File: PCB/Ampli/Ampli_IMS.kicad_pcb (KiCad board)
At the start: 2 copper layers, 58.4 x 32 mm, 18 parts, among them J1 5227161-3, J2 5227161-3, J3 Conn_01x03_Male, P1 300K, U1 LMC6081, U2 LMC6081

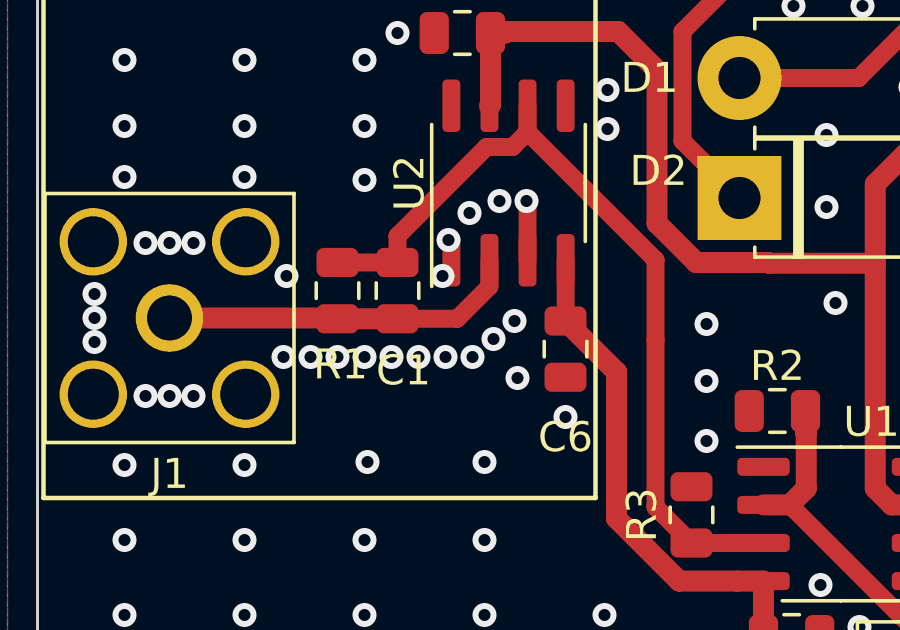
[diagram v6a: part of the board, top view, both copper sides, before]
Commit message: Small mistakes
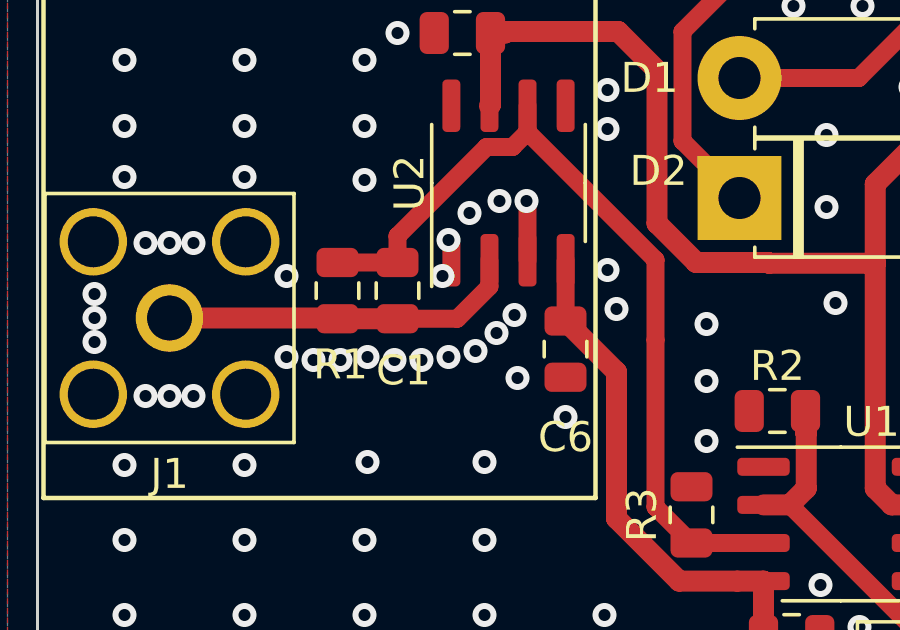
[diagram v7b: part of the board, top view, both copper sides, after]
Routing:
- net GND: vias 151 -> 153
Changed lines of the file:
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@@
     (thickness 1.6)
     (drawings 15)
-    (tracks 228)
+    (tracks 230)
     (zones 0)
     (modules 18)
@@
   )
   (setup
-    (last_trace_width 0.6)
+    (last_trace_width 0.25)
     (user_trace_width 0.4)
     (user_trace_width 0.5)
@@
   (via blind (at 36.6 24.5) (size 0.8) (drill 0.4) (layers F.Cu B.Cu) (net 1))
   (via blind (at 43.6 27.7) (size 0.8) (drill 0.4) (layers F.Cu B.Cu) (net 1))
-  (via (at 36.4 35.3) (size 0.8) (drill 0.4) (layers F.Cu B.Cu) (net 1))
-  (via (at 35.5 35.3) (size 0.8) (drill 0.4) (layers F.Cu B.Cu) (net 1))
+  (via (at 36.5 35.4) (size 0.8) (drill 0.4) (layers F.Cu B.Cu) (net 1))
+  (via (at 35.6 35.3) (size 0.8) (drill 0.4) (layers F.Cu B.Cu) (net 1))
   (via blind (at 79.5 30.3) (size 0.8) (drill 0.4) (layers F.Cu B.Cu) (net 1))
   (via blind (at 75.5 32.8) (size 0.8) (drill 0.4) (layers F.Cu B.Cu) (net 1))
@@
   (segment (start 40.935 32.075) (end 40.935 30.065) (width 0.6) (layer F.Cu) (net 1))
   (segment (start 40.935 30.065) (end 40.935 30.035) (width 0.6) (layer F.Cu) (net 1))
-  (via (at 37.3 35.3) (size 0.8) (drill 0.4) (layers F.Cu B.Cu) (net 1))
-  (via (at 38.2 35.3) (size 0.8) (drill 0.4) (layers F.Cu B.Cu) (net 1))
-  (via (at 39.1 35.3) (size 0.8) (drill 0.4) (layers F.Cu B.Cu) (net 1))
+  (via (at 37.4 35.4) (size 0.8) (drill 0.4) (layers F.Cu B.Cu) (net 1))
+  (via (at 38.3 35.3) (size 0.8) (drill 0.4) (layers F.Cu B.Cu) (net 1))
+  (via (at 39.2 35.1) (size 0.8) (drill 0.4) (layers F.Cu B.Cu) (net 1))
   (via (at 28.2 36.6) (size 0.8) (drill 0.4) (layers F.Cu B.Cu) (net 1))
   (via (at 26.5 33.2) (size 0.8) (drill 0.4) (layers F.Cu B.Cu) (net 1))
@@
   (via blind (at 46.9 34.2) (size 0.8) (drill 0.4) (layers F.Cu B.Cu) (net 1))
   (via blind (at 46.9 36.1) (size 0.8) (drill 0.4) (layers F.Cu B.Cu) (net 1))
-  (via (at 39.8 34.7) (size 0.8) (drill 0.4) (layers F.Cu B.Cu) (net 1))
-  (via (at 34.6 35.3) (size 0.8) (drill 0.4) (layers F.Cu B.Cu) (net 1))
+  (via (at 39.9 34.5) (size 0.8) (drill 0.4) (layers F.Cu B.Cu) (net 1))
+  (via (at 34.7 35.4) (size 0.8) (drill 0.4) (layers F.Cu B.Cu) (net 1))
   (via blind (at 35.5 29.4) (size 0.8) (drill 0.4) (layers F.Cu B.Cu) (net 1))
   (via blind (at 55.1 32.7) (size 0.8) (drill 0.4) (layers F.Cu B.Cu) (net 1))
@@
   (via blind (at 42.2 37.3) (size 0.8) (drill 0.4) (layers F.Cu B.Cu) (net 1))
   (via blind (at 51.2 33.5) (size 0.8) (drill 0.4) (layers F.Cu B.Cu) (net 1))
-  (via (at 33.7 35.3) (size 0.8) (drill 0.4) (layers F.Cu B.Cu) (net 1))
-  (via (at 32.8 35.3) (size 0.8) (drill 0.4) (layers F.Cu B.Cu) (net 1))
+  (via (at 33.8 35.4) (size 0.8) (drill 0.4) (layers F.Cu B.Cu) (net 1))
+  (via (at 32.9 35.3) (size 0.8) (drill 0.4) (layers F.Cu B.Cu) (net 1))
   (via (at 29 36.6) (size 0.8) (drill 0.4) (layers F.Cu B.Cu) (net 1))
   (via (at 26.5 34) (size 0.8) (drill 0.4) (layers F.Cu B.Cu) (net 1))
@@
   (via (at 39 30.5) (size 0.8) (drill 0.4) (layers F.Cu B.Cu) (net 1))
   (via (at 40 30.1) (size 0.8) (drill 0.4) (layers F.Cu B.Cu) (net 1))
-  (via (at 40.5 34.1) (size 0.8) (drill 0.4) (layers F.Cu B.Cu) (net 1))
+  (via (at 40.5 33.9) (size 0.8) (drill 0.4) (layers F.Cu B.Cu) (net 1))
   (via blind (at 35.5 25.4) (size 0.8) (drill 0.4) (layers F.Cu B.Cu) (net 1))
   (via blind (at 35.5 27.6) (size 0.8) (drill 0.4) (layers F.Cu B.Cu) (net 1))
   (via blind (at 56.4 37) (size 0.8) (drill 0.4) (layers F.Cu B.Cu) (net 1))
   (via blind (at 57.8 38.3) (size 0.8) (drill 0.4) (layers F.Cu B.Cu) (net 1))
+  (via blind (at 43.6 32.4) (size 0.8) (drill 0.4) (layers F.Cu B.Cu) (net 1))
+  (via blind (at 43.9 33.7) (size 0.8) (drill 0.4) (layers F.Cu B.Cu) (net 1))
   (segment (start 51.975 26) (end 56 21.975) (width 0.6) (layer F.Cu) (net 2))
   (segment (start 56 21.975) (end 56 21) (width 0.6) (layer F.Cu) (net 2))
@@
   (segment (start 45.19999 32.06499) (end 40.935 27.8) (width 0.6) (layer F.Cu) (net 7))
   (segment (start 45.19999 34.72999) (end 45.19999 32.06499) (width 0.6) (layer F.Cu) (net 7))
-  (segment (start 54.3 44.927208) (end 54.3 46.2) (width 0.6) (layer F.Cu) (net 9))
-  (segment (start 49.675 40.23) (end 54.3 44.855) (width 0.6) (layer F.Cu) (net 9))
-  (segment (start 54.3 44.855) (end 54.3 44.927208) (width 0.5) (layer F.Cu) (net 9))
   (segment (start 66.195 34.08) (end 70 34.08) (width 0.6) (layer F.Cu) (net 8))
   (segment (start 56.8 43.475) (end 66.195 34.08) (width 0.6) (layer F.Cu) (net 8))
@@
   (segment (start 54.825 41.5) (end 53.95 41.5) (width 0.6) (layer F.Cu) (net 8))
   (segment (start 56.8 43.475) (end 54.825 41.5) (width 0.6) (layer F.Cu) (net 8))
+  (segment (start 54.3 44.927208) (end 54.3 46.2) (width 0.6) (layer F.Cu) (net 9))
+  (segment (start 49.675 40.23) (end 54.3 44.855) (width 0.6) (layer F.Cu) (net 9))
+  (segment (start 54.3 44.855) (end 54.3 44.927208) (width 0.5) (layer F.Cu) (net 9))
   (segment (start 50.22501 37.82501) (end 50.2 37.8) (width 0.7) (layer F.Cu) (net 9))
   (segment (start 50.22501 39.67999) (end 50.22501 37.82501) (width 0.7) (layer F.Cu) (net 9))
@@
     (polygon
       (pts
-        (xy 41.5 33.15) (xy 40.3 33.2) (xy 38.7 34.8) (xy 35.6 34.8) (xy 35.3 34.8)
-        (xy 34 34.8) (xy 33.75 34.8) (xy 30.8 34.8) (xy 29.9 35.6) (xy 28.1 35.6)
-        (xy 27.1 34) (xy 28.1 32.3) (xy 29.9 32.3) (xy 30.8 33.2) (xy 33.7 33.2)
-        (xy 34 33.2) (xy 35.3 33.2) (xy 35.7 33.2) (xy 38.6 33.15) (xy 39 32.85)
-        (xy 39 30.7) (xy 41.5 30.7)
+        (xy 41.5 33.15) (xy 40.3 33.2) (xy 38.7 34.8) (xy 37.5 34.8) (xy 37.1 35)
+        (xy 36.05 35) (xy 35.6 34.8) (xy 35.1 35) (xy 34 35) (xy 33.75 34.8)
+        (xy 30.8 34.8) (xy 29.9 35.6) (xy 28.1 35.6) (xy 27.1 34) (xy 28.1 32.3)
+        (xy 29.9 32.3) (xy 30.8 33.2) (xy 33.7 33.2) (xy 34 33.2) (xy 35.3 33.2)
+        (xy 35.7 33.2) (xy 38.6 33.15) (xy 39 32.85) (xy 39 30.7) (xy 41.5 30.7)
       )
     )

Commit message: GND guards are neat!
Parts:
- removed C6, C7: 0.1uF, Capacitor_SMD:C_0805_2012Metric
- removed U2: LMC6081, Package_SO:SO-8_3.9x4.9mm_P1.27mm
- C2, C5: value 47uF Tant -> 0.1uF; footprint Capacitor_THT:CP_Radial_Tantal_D5.0mm_P5.00mm -> Capacitor_SMD:C_0805_2012Metric
- C3, C4: value 0.1uF -> 47uF Tant; footprint Capacitor_SMD:C_0805_2012Metric -> Capacitor_THT:CP_Radial_Tantal_D5.0mm_P5.00mm
- U1: value LMC6081 -> LMC6082
- moved C4 27.0 mm to (65.5, 20.7)
- moved C5 26.3 mm to (37.9, 30.1), turned to 180 degrees
- moved P1 23.0 mm to (31.3, 45.9)
- moved C2 21.9 mm to (45.3, 37.4), turned to 0 degrees
- moved J3 14.4 mm to (41.6, 21.1)
- moved J2 14.0 mm to (56.3, 37.1), turned to 180 degrees
- moved C3 13.7 mm to (60.5, 26.3), turned to 0 degrees
- moved U1 12.3 mm to (40.7, 34.8), turned to 270 degrees
- moved R2 10.5 mm to (39.1, 39.5)
- moved D2 9.38 mm to (46.8, 20.7)
- moved R3 8.46 mm to (45.1, 32.2), turned to 0 degrees
- moved C1 1.82 mm to (36.8, 34.9), turned to 90 degrees
- moved R1 1.81 mm to (34.6, 34.9), turned to 90 degrees
- moved D1 1.41 mm to (57.0, 25.2)
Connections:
- C4 pad 1: /+5V -> GND
- C4 pad 2: GND -> /-5V
- C5 pad 1: GND -> /-5V
- C5 pad 2: /-5V -> GND
- P1 pad 3: Net-(P1-Pad3) -> Net-(J2-Pad1)
- U1 pad 1: (no net) -> Net-(C1-Pad1)
- U1 pad 2: Net-(P1-Pad1) -> Net-(C1-Pad2)
- U1 pad 3: Net-(C1-Pad1) -> GND
- U1 pad 5: (no net) -> Net-(C1-Pad1)
- U1 pad 6: Net-(J2-Pad1) -> Net-(P1-Pad1)
- U1 pad 7: /+5V -> Net-(J2-Pad1)
- U1 pad 8: (no net) -> /+5V
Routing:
- net /-5V: track 66.5 -> 27.8 mm
- net /+5V: track 48.6 -> 23.4 mm
- net Net-(C1-Pad1): track 27.9 -> 15.1 mm
- net Net-(J2-Pad1): track 23.5 -> 29.9 mm
- net Net-(D1-Pad2): track 10.6 -> 6.94 mm
- net GND: track 2.04 -> 0.00 mm, vias 153 -> 36
- net Net-(C1-Pad2): track 12.0 -> 13.6 mm
- net Net-(P1-Pad1): track 12.1 -> 13.6 mm
- net Net-(D2-Pad1): track 12.7 -> 11.4 mm
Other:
- board size 58.4 x 32 mm -> 44.4 x 32 mm
- board text removed: "+5V"
- board text removed: "-5V"
- board text removed: "Critical part : Transimpedance amp"
